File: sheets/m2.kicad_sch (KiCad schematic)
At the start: 50 parts, among them CN1 EM92xx / RM520N M.2 Key-B (67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, Q1 2N7002, Q2 2N7002, Q3 2N7002, Q4 2N7002, Q5 2N7002

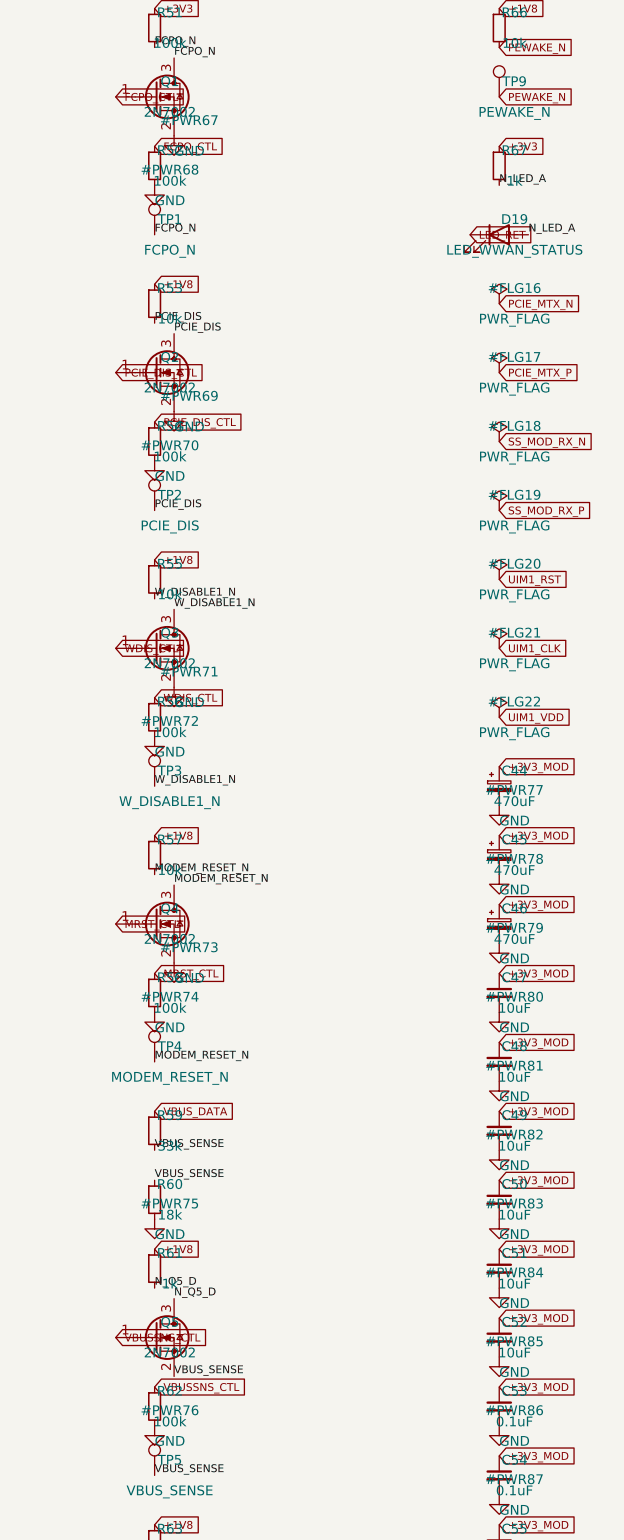
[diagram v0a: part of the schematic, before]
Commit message: sch: m2 fixes — P-FET VBUS_SENSE force path, 1% divider, WWAN LED through module pin
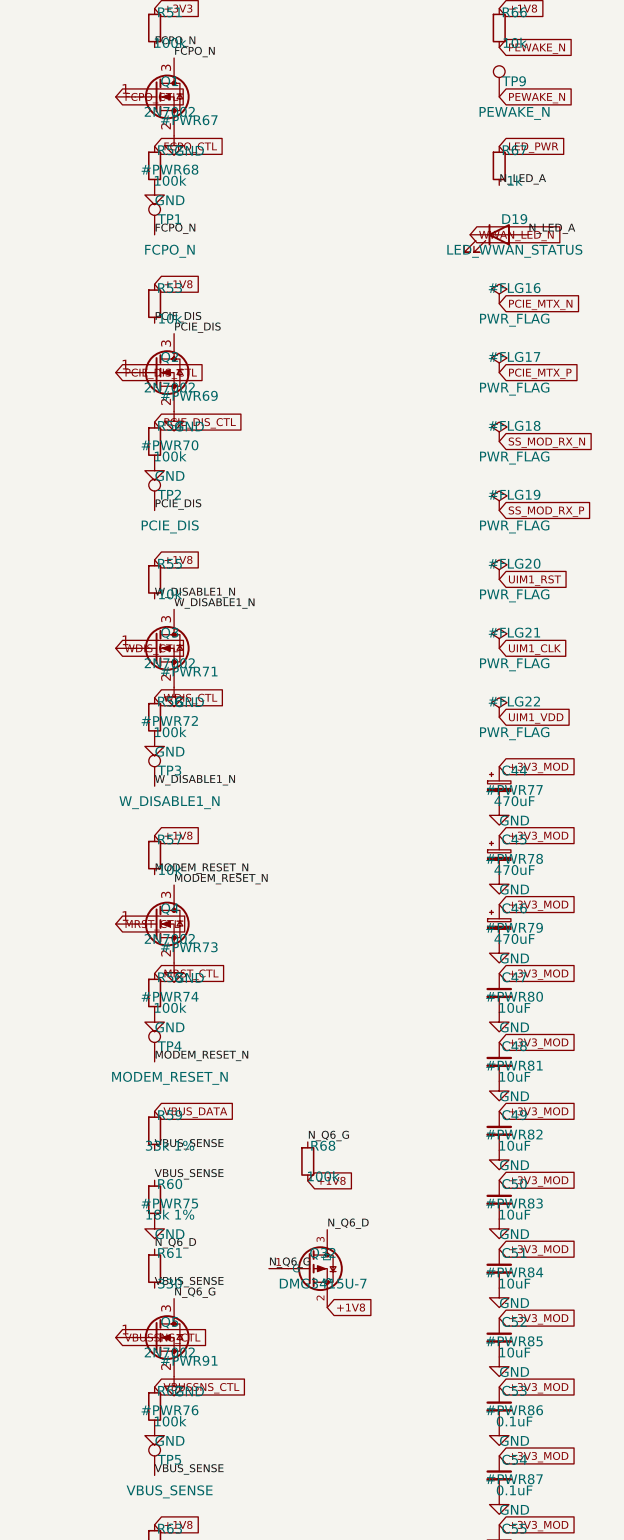
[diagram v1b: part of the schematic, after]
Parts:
- added Q32: DMG3415U-7, Package_TO_SOT_SMD:SOT-23, symbol sierra-to-usb:DMG3415U
- added R68: 100k, Resistor_SMD:R_0603_1608Metric, symbol Device:R_Small
- C44, C45, C46: footprint CP_Elec_6.3x7.7 -> Capacitor_SMD:CP_Elec_6.3x7.7
- C47, C48, C49, C50, C51, C52: footprint C_0805_2012Metric -> Capacitor_SMD:C_0805_2012Metric
- C53, C54, C55, C56, C57: footprint C_0402_1005Metric -> Capacitor_SMD:C_0402_1005Metric
- R59: value 33k -> 33k 1%
- R60: value 18k -> 18k 1%
- R61: value 1k -> 330
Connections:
- net LED_RET is gone; now on net WWAN_LED_N: D19.1 (K)
- net +1V8: now also Q32.2 (S), R68.2; no longer R61.1
- net +3V3: no longer R67.1
- net GND: now also Q5.2 (S)
- net VBUS_SENSE: now also R61.2; no longer Q5.2 (S)
- net N_Q5_D renamed N_Q6_G
- net N_Q6_G: now also Q32.1 (G), R68.1; no longer R61.2
- new net LED_PWR: R67.1
- new net N_Q6_D: Q32.3 (D), R61.1
